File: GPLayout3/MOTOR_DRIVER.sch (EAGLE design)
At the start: 94 parts, among them T1 2N2222, T2 2N2222, U7 ATMEGA328P_TQFP, Y1 16MHz

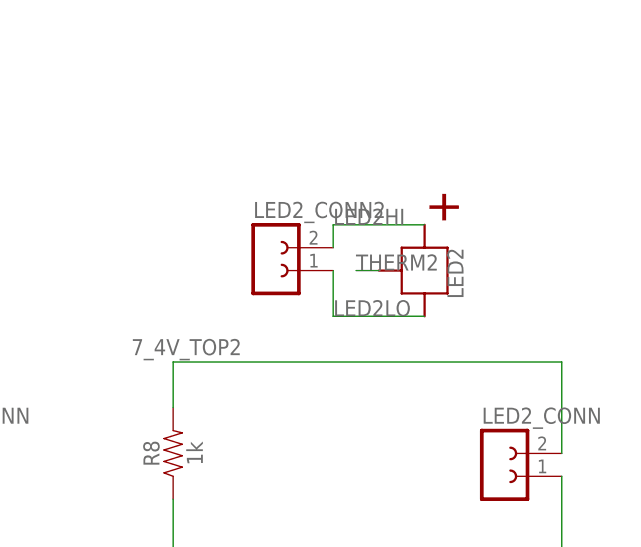
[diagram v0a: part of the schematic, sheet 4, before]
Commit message: changed some drill sizes to .8 instead of .6. fixed some clearance issues with LED
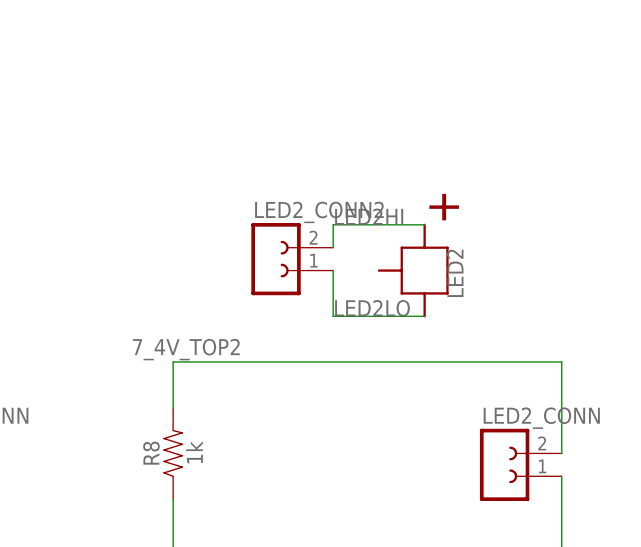
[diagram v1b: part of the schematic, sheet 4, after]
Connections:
- removed net THERM2: LED2.THERMAL
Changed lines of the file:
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@@
 <?xml version="1.0" encoding="utf-8"?>
 <!DOCTYPE eagle SYSTEM "eagle.dtd">
-<eagle version="8.0.0">
+<eagle version="8.0.1">
 <drawing>
 <settings>
@@
 </segment>
 </net>
-<net name="THERM2" class="0">
-<segment>
-<pinref part="LED2" gate="G$1" pin="THERMAL"/>
-<wire x1="309.88" y1="215.9" x2="307.34" y2="215.9" width="0.1524" layer="91"/>
-<label x="307.34" y="215.9" size="1.778" layer="95"/>
-</segment>
-</net>
